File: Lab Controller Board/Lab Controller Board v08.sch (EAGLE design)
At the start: 47 parts, among them Q2 MMBT5088, Q3 100A/100V, Q4 MMBT5088, Q5 100A/100V, Q6 MMBT5088, Q7 100A/100V, Q8 MMBT5088, U1 ATMEGA328P_TQFP, U2 CH340G, U3 +12v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

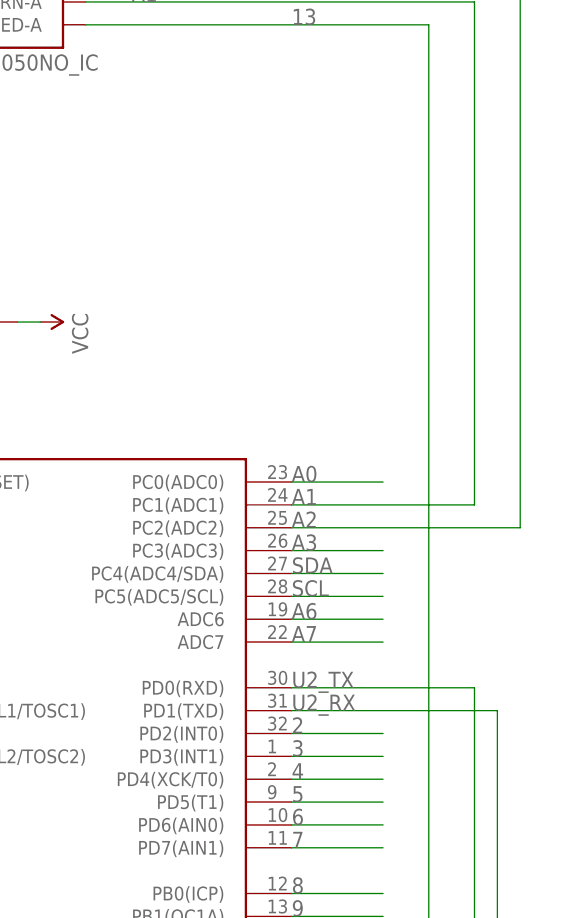
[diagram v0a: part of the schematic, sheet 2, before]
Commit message: Added ESP-07, RX/TX level converter, temp probe connection.  Cleaned silkscreen
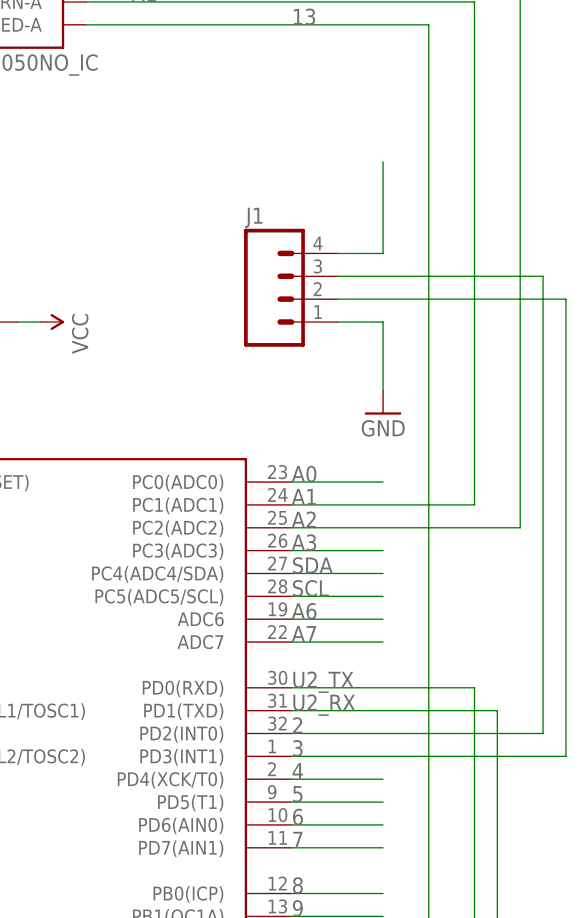
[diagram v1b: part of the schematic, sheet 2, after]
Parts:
- added J1: (no value), SparkFun-Connectors:M04LOCK
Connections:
- net 2: now also J1.3
- net 3: now also J1.2
- net GND: now also J1.1
- net VCC: now also J1.4
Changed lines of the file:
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@@
 <grid distance="0.1" unitdist="inch" unit="inch" style="lines" multiple="1" display="no" altdistance="0.01" altunitdist="inch" altunit="inch"/>
 <layers>
-<layer number="1" name="Top" color="4" fill="1" visible="yes" active="no"/>
-<layer number="16" name="Bottom" color="1" fill="1" visible="yes" active="no"/>
-<layer number="17" name="Pads" color="2" fill="1" visible="yes" active="no"/>
-<layer number="18" name="Vias" color="2" fill="1" visible="yes" active="no"/>
-<layer number="19" name="Unrouted" color="6" fill="1" visible="yes" active="no"/>
-<layer number="20" name="Dimension" color="15" fill="1" visible="yes" active="no"/>
-<layer number="21" name="tPlace" color="7" fill="1" visible="yes" active="no"/>
-<layer number="22" name="bPlace" color="7" fill="1" visible="yes" active="no"/>
-<layer number="23" name="tOrigins" color="15" fill="1" visible="yes" active="no"/>
-<layer number="24" name="bOrigins" color="15" fill="1" visible="yes" active="no"/>
-<layer number="25" name="tNames" color="7" fill="1" visible="yes" active="no"/>
-<layer number="26" name="bNames" color="7" fill="1" visible="yes" active="no"/>
-<layer number="27" name="tValues" color="7" fill="1" visible="yes" active="no"/>
-<layer number="28" name="bValues" color="7" fill="1" visible="yes" active="no"/>
+<layer number="1" name="Top" color="4" fill="1" visible="no" active="no"/>
+<layer number="16" name="Bottom" color="1" fill="1" visible="no" active="no"/>
+<layer number="17" name="Pads" color="2" fill="1" visible="no" active="no"/>
+<layer number="18" name="Vias" color="2" fill="1" visible="no" active="no"/>
+<layer number="19" name="Unrouted" color="6" fill="1" visible="no" active="no"/>
+<layer number="20" name="Dimension" color="15" fill="1" visible="no" active="no"/>
+<layer number="21" name="tPlace" color="7" fill="1" visible="no" active="no"/>
+<layer number="22" name="bPlace" color="7" fill="1" visible="no" active="no"/>
+<layer number="23" name="tOrigins" color="15" fill="1" visible="no" active="no"/>
+<layer number="24" name="bOrigins" color="15" fill="1" visible="no" active="no"/>
+<layer number="25" name="tNames" color="7" fill="1" visible="no" active="no"/>
+<layer number="26" name="bNames" color="7" fill="1" visible="no" active="no"/>
+<layer number="27" name="tValues" color="7" fill="1" visible="no" active="no"/>
+<layer number="28" name="bValues" color="7" fill="1" visible="no" active="no"/>
 <layer number="29" name="tStop" color="7" fill="3" visible="no" active="no"/>
 <layer number="30" name="bStop" color="7" fill="6" visible="no" active="no"/>
@@
 <layer number="35" name="tGlue" color="7" fill="4" visible="no" active="no"/>
 <layer number="36" name="bGlue" color="7" fill="5" visible="no" active="no"/>
-<layer number="37" name="tTest" color="7" fill="1" visible="yes" active="no"/>
-<layer number="38" name="bTest" color="7" fill="1" visible="yes" active="no"/>
+<layer number="37" name="tTest" color="7" fill="1" visible="no" active="no"/>
+<layer number="38" name="bTest" color="7" fill="1" visible="no" active="no"/>
 <layer number="39" name="tKeepout" color="4" fill="11" visible="no" active="no"/>
 <layer number="40" name="bKeepout" color="1" fill="11" visible="no" active="no"/>
@@
 <layer number="44" name="Drills" color="7" fill="1" visible="no" active="no"/>
 <layer number="45" name="Holes" color="7" fill="1" visible="no" active="no"/>
-<layer number="46" name="Milling" color="3" fill="1" visible="yes" active="no"/>
-<layer number="47" name="Measures" color="7" fill="1" visible="yes" active="no"/>
-<layer number="48" name="Document" color="7" fill="1" visible="yes" active="no"/>
-<layer number="49" name="Reference" color="7" fill="1" visible="yes" active="no"/>
-<layer number="50" name="dxf" color="7" fill="1" visible="yes" active="no"/>
-<layer number="51" name="tDocu" color="7" fill="1" visible="yes" active="no"/>
-<layer number="52" name="bDocu" color="7" fill="1" visible="yes" active="no"/>
-<layer number="53" name="tGND_GNDA" color="7" fill="9" visible="yes" active="no"/>
-<layer number="54" name="bGND_GNDA" color="1" fill="9" visible="yes" active="no"/>
-<layer number="56" name="wert" color="7" fill="1" visible="yes" active="no"/>
-<layer number="57" name="tCAD" color="7" fill="1" visible="yes" active="no"/>
-<layer number="59" name="tCarbon" color="7" fill="1" visible="yes" active="no"/>
-<layer number="60" name="bCarbon" color="7" fill="1" visible="yes" active="no"/>
+<layer number="46" name="Milling" color="3" fill="1" visible="no" active="no"/>
+<layer number="47" name="Measures" color="7" fill="1" visible="no" active="no"/>
+<layer number="48" name="Document" color="7" fill="1" visible="no" active="no"/>
+<layer number="49" name="Reference" color="7" fill="1" visible="no" active="no"/>
+<layer number="50" name="dxf" color="7" fill="1" visible="no" active="no"/>
+<layer number="51" name="tDocu" color="7" fill="1" visible="no" active="no"/>
+<layer number="52" name="bDocu" color="7" fill="1" visible="no" active="no"/>
+<layer number="53" name="tGND_GNDA" color="7" fill="9" visible="no" active="no"/>
+<layer number="54" name="bGND_GNDA" color="1" fill="9" visible="no" active="no"/>
+<layer number="56" name="wert" color="7" fill="1" visible="no" active="no"/>
+<layer number="57" name="tCAD" color="7" fill="1" visible="no" active="no"/>
+<layer number="59" name="tCarbon" color="7" fill="1" visible="no" active="no"/>
+<layer number="60" name="bCarbon" color="7" fill="1" visible="no" active="no"/>
 <layer number="90" name="Modules" color="5" fill="1" visible="yes" active="yes"/>
 <layer number="91" name="Nets" color="2" fill="1" visible="yes" active="yes"/>
@@
 <part name="CN1" library="adafruit" deviceset="USB" device="MINIB"/>
 <part name="U3" library="SparkFun-PowerIC" deviceset="V_REG_78XX" device="7812" value="+12v"/>
+<part name="J1" library="SparkFun-Connectors" deviceset="M04" device="LOCK"/>
+<part name="GND15" library="SparkFun-Aesthetics" deviceset="GND" device=""/>
 </parts>
 <sheets>
@@
 <instance part="CN1" gate="G$1" x="101.6" y="22.86"/>
 <instance part="U3" gate="G$1" x="71.12" y="116.84"/>
+<instance part="J1" gate="G$1" x="213.36" y="73.66"/>
+<instance part="GND15" gate="1" x="223.52" y="60.96" rot="MR0"/>
 </instances>
 <busses>
@@
 <wire x1="71.12" y1="109.22" x2="71.12" y2="106.68" width="0.1524" layer="91"/>
 <pinref part="U3" gate="G$1" pin="GND"/>
+</segment>
+<segment>
+<pinref part="J1" gate="G$1" pin="1"/>
+<wire x1="218.44" y1="71.12" x2="223.52" y2="71.12" width="0.1524" layer="91"/>
+<wire x1="223.52" y1="71.12" x2="223.52" y2="63.5" width="0.1524" layer="91"/>
+<pinref part="GND15" gate="1" pin="GND"/>
 </segment>
 </net>
@@
 <label x="111.76" y="27.94" size="1.778" layer="95"/>
 </segment>
+<segment>
+<pinref part="J1" gate="G$1" pin="4"/>
+<wire x1="218.44" y1="78.74" x2="223.52" y2="78.74" width="0.1524" layer="91"/>
+<wire x1="223.52" y1="78.74" x2="223.52" y2="88.9" width="0.1524" layer="91"/>
+</segment>
 </net>
 <net name="N$1" class="0">
@@
 <net name="3" class="0">
 <segment>
-<wire x1="213.36" y1="22.86" x2="223.52" y2="22.86" width="0.1524" layer="91"/>
 <pinref part="U1" gate="U$1" pin="PD3(INT1)"/>
 <label x="213.36" y="22.86" size="1.778" layer="95"/>
+<pinref part="J1" gate="G$1" pin="2"/>
+<wire x1="218.44" y1="73.66" x2="243.84" y2="73.66" width="0.1524" layer="91"/>
+<wire x1="243.84" y1="73.66" x2="243.84" y2="22.86" width="0.1524" layer="91"/>
+<wire x1="243.84" y1="22.86" x2="213.36" y2="22.86" width="0.1524" layer="91"/>
 </segment>
 </net>
 <net name="2" class="0">
 <segment>
-<wire x1="213.36" y1="25.4" x2="223.52" y2="25.4" width="0.1524" layer="91"/>
 <pinref part="U1" gate="U$1" pin="PD2(INT0)"/>
 <label x="213.36" y="25.4" size="1.778" layer="95"/>
-</segment>
-</net>
+<wire x1="213.36" y1="25.4" x2="241.3" y2="25.4" width="0.1524" layer="91"/>
+<wire x1="241.3" y1="25.4" x2="241.3" y2="76.2" width="0.1524" layer="91"/>
+<pinref part="J1" gate="G$1" pin="3"/>
+<wire x1="241.3" y1="76.2" x2="218.44" y2="76.2" width="0.1524" layer="91"/>
+</segment>
+</net>
